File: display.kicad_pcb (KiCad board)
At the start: 2 copper layers, 154.4 x 18.8 mm, 43 parts, among them P1 USB, P10 NAV_TRANS, P11 NAV_ID, P12 NAV_VOL, P2 Power, P3 SPI Debug, P4 LED_JUMPER, P5 COM_ENC, P6 COM_STEP, P7 COM_TRANS, P8 COM_VOL, P9 NAV_ENC, U1 ATmega32U4, U10 RESET, U2 MAX7221, U3 5x7Segment, U4 MAX7221, U5 5x7Segment, U6 MAX7221, U7 5x7Segment, U8 MAX7221, U9 5x7Segment

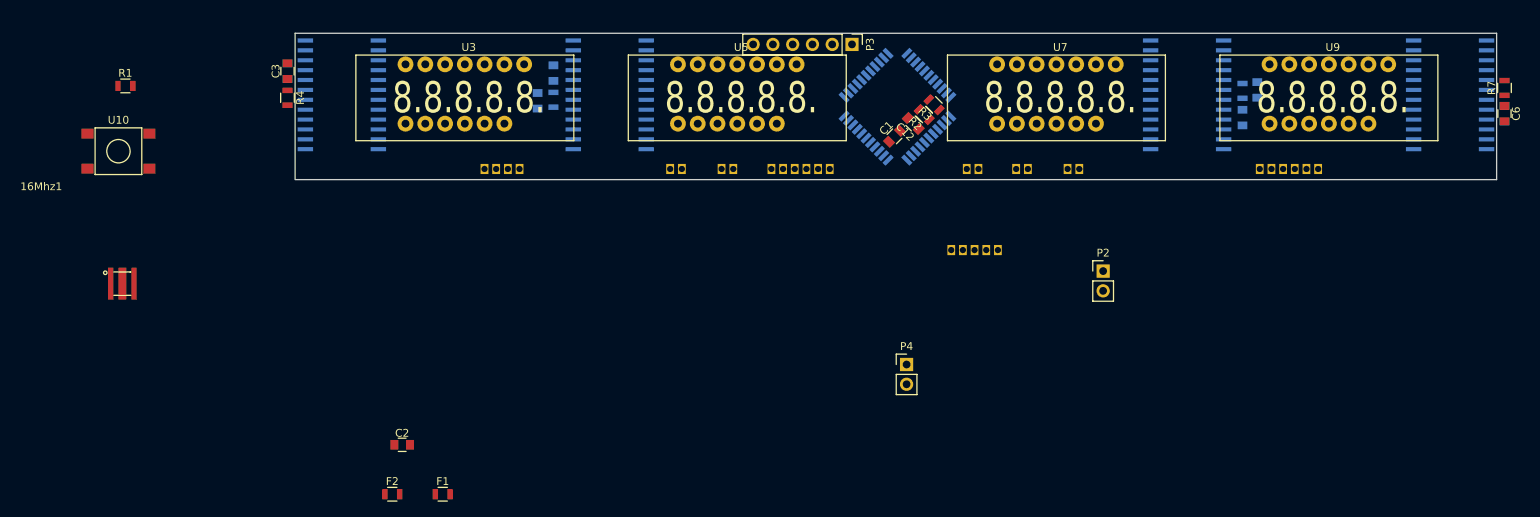
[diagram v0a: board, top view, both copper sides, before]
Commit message: Finished trace routing.  Added 3d parts
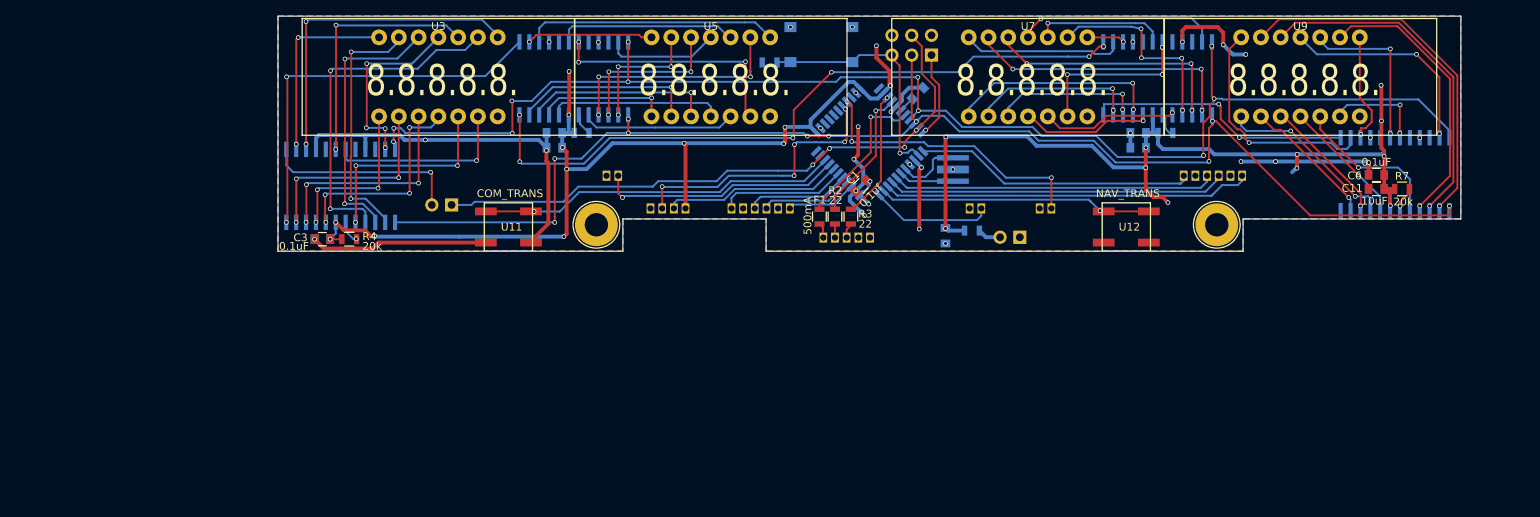
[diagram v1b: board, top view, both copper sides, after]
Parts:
- removed P10: NAV_TRANS, custom:JST-ZH-THRx2
- removed P7: COM_TRANS, custom:JST-ZH-THRx2
- added Ref**: Val**, custom:SCREW_4-40, F.Cu at (140.9, 126.8)
- added Ref**: Val**, custom:SCREW_4-40, F.Cu at (220.6, 126.8)
- added U11: COM_TRANS, custom:TAC_SWITCH_CK_KSC4_JWING, F.Cu at (129.6, 127.1)
- added U12: NAV_TRANS, custom:TAC_SWITCH_CK_KSC4_JWING, F.Cu at (209.0, 127.1)
- 16Mhz1, C12, C2, F2, R1, U10: moved to B.Cu
- C11: moved to F.Cu
- P2, P4: footprint Pin_Headers:Pin_Header_Straight_1x02_Pitch2.54mm -> custom:Pin_Header_Straight_1x02_Pitch2.54mm; moved to B.Cu
- P3: footprint Pin_Headers:Pin_Header_Straight_1x06_Pitch2.54mm -> custom:Pin_Header_Straight_2x03_Pitch2.54mm; moved to B.Cu
- U3, U5, U7, U9: value 5x7Segment -> 5x7Segment_0.36; footprint custom:5x7Segment -> custom:5x7Segment_0.36
- moved 16Mhz1 107.7 mm to (186.7, 119.7), turned to 90 degrees
- moved U10 91.3 mm to (169.8, 103.7)
- moved R1 82.8 mm to (163.2, 106.0), turned to 180 degrees
- moved F2 81.8 mm to (189.2, 127.5), turned to 180 degrees
- moved C2 74.8 mm to (185.8, 128.2), turned to 270 degrees
- moved P4 61.9 mm to (122.3, 124.2), turned to 90 degrees
- moved F1 60.1 mm to (169.6, 125.8), turned to 90 degrees
- moved C3 22.0 mm to (105.7, 128.7), turned to 180 degrees
- moved C8 22.0 mm to (105.7, 128.7), turned to 180 degrees
- moved P8 21.9 mm to (150.1, 124.7)
- moved R4 19.8 mm to (109.2, 128.7), turned to 0 degrees
- moved C11 19.1 mm to (241.1, 122.2), turned to 180 degrees
- moved R7 18.5 mm to (244.4, 122.2), turned to 0 degrees
- moved C6 18.2 mm to (241.1, 120.4), turned to 180 degrees
- moved R3 17.9 mm to (173.6, 125.8), turned to 270 degrees
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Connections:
- U1 pad 12: /COM_S_B -> /NAV_S_B
- U1 pad 18: /COM_PWR -> /NAV_S_A
- U1 pad 19: /NAV_L_A -> /NAV_L_B
- U1 pad 20: /NAV_L_B -> /NAV_L_A
- U1 pad 21: /NAV_S_A -> /NAV_TRANS
- U1 pad 22: /NAV_TRANS -> /NAV_ID
- U1 pad 25: /NAV_S_B -> /COM_L_A
- U1 pad 26: /NAV_ID -> /COM_L_B
- U1 pad 27: (no net) -> /COM_S_A
- U1 pad 28: /COM_L_A -> /COM_S_B
- U1 pad 29: /COM_L_B -> /COM_PWR
- U1 pad 30: /COM_S_A -> /COM_STEP
- U1 pad 31: /COM_STEP -> /COM_TRANS
- U1 pad 32: /COM_TRANS -> (no net)
- U1 pad 40: /NAV_VOL -> /COM_VOL
- U1 pad 41: /COM_VOL -> /NAV_VOL
- U10 pad 1: GND -> /RST
- U10 pad 4: /RST -> GND
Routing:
- net VCC: track 0.00 -> 253.3 mm, vias 0 -> 30
- net CS: track 0.00 -> 175.0 mm, vias 0 -> 11
- net CLK: track 0.00 -> 172.5 mm, vias 0 -> 10
- net GND: track 0.00 -> 114.8 mm, vias 0 -> 25
- net /NavActive/DIN: track 0.00 -> 90.1 mm, vias 0 -> 6
- net /MOSI: track 0.00 -> 79.0 mm, vias 0 -> 4
- net /ComStandby/DIN: track 0.00 -> 50.6 mm, vias 0 -> 2
- net /NAV_L_A: track 0.00 -> 47.5 mm
- net /NavStandby/S_A: track 0.00 -> 46.9 mm, vias 0 -> 1
- net /COM_TRANS: track 0.00 -> 46.3 mm, vias 0 -> 1
- net /ComActive/S_B: track 0.00 -> 44.5 mm, vias 0 -> 2
- net /NavStandby/S_F: track 0.00 -> 43.7 mm, vias 0 -> 1
- net /NAV_L_B: track 0.00 -> 43.5 mm
- net /ComActive/D_5: track 0.00 -> 42.2 mm, vias 0 -> 2
- net /NAV_S_A: track 0.00 -> 41.7 mm
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- added copper zone on F.Cu, net GND
- added copper zone on B.Cu, net VCC
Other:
- board size 154.4 x 18.8 mm -> 151.9 x 30.2 mm
- net class Power added: clearance 0.2, trace_width 0.5, via_dia 0.6, via_drill 0.4

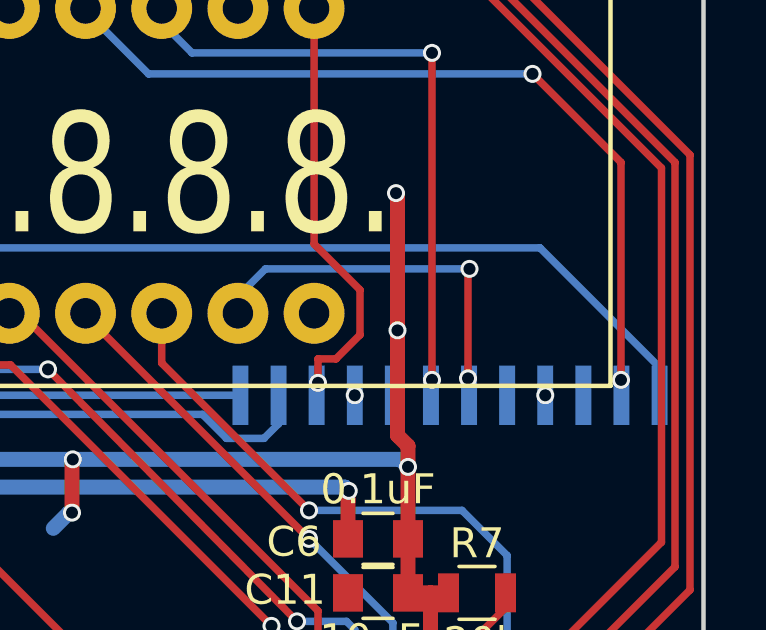
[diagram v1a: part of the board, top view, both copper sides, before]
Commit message: Fixed unconnected ground.
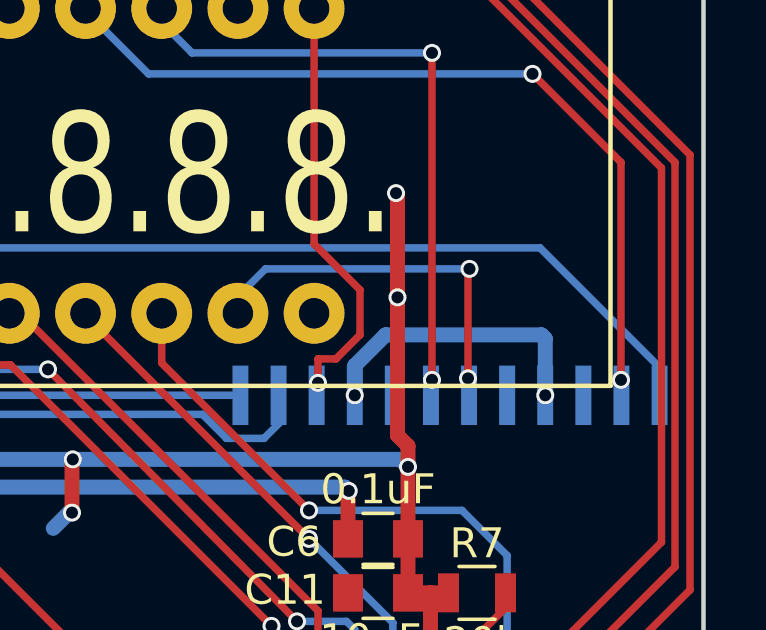
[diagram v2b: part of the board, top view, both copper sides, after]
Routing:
- net GND: track 114.8 -> 124.5 mm
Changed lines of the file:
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@@
   (general
     (links 170)
-    (no_connects 1)
+    (no_connects 0)
     (area 99.924999 99.924999 252.025001 130.275001)
     (thickness 1.6)
     (drawings 11)
-    (tracks 1115)
+    (tracks 1120)
     (zones 0)
     (modules 45)
@@
   (page A4)
   (layers
-    (0 F.Cu signal hide)
+    (0 F.Cu signal)
     (31 B.Cu signal)
     (32 B.Adhes user)
@@
   (segment (start 192.76 128.4) (end 190.95 128.4) (width 0.5) (layer B.Cu) (net 1))
   (segment (start 190.95 128.4) (end 190.1 127.55) (width 0.5) (layer B.Cu) (net 1))
+  (segment (start 246.675 115.6135) (end 246.675 113.725) (width 0.5) (layer B.Cu) (net 2))
+  (segment (start 241.35 113.6) (end 240.325 114.625) (width 0.5) (layer B.Cu) (net 2))
+  (segment (start 246.55 113.6) (end 241.35 113.6) (width 0.5) (layer B.Cu) (net 2))
+  (segment (start 246.675 113.725) (end 246.55 113.6) (width 0.5) (layer B.Cu) (net 2))
+  (segment (start 240.325 114.625) (end 240.325 115.6135) (width 0.5) (layer B.Cu) (net 2))
+  (segment (start 246.675 115.6135) (end 246.675 115.625) (width 0.5) (layer F.Cu) (net 2))
+  (via (at 246.675 115.6135) (size 0.6) (drill 0.4) (layers F.Cu B.Cu) (net 2))
+  (via (at 240.325 115.6135) (size 0.6) (drill 0.4) (layers F.Cu B.Cu) (net 2))
   (segment (start 216.175 103.3135) (end 216.175 101.85) (width 0.5) (layer F.Cu) (net 2))
   (segment (start 216.175 103.3) (end 216.175 103.3135) (width 0.5) (layer F.Cu) (net 2))
@@
   (via (at 240.125 118.8) (size 0.6) (drill 0.4) (layers F.Cu B.Cu) (net 2))
   (segment (start 240.1 118.825) (end 240.125 118.8) (width 0.5) (layer F.Cu) (net 2))
-  (via (at 246.675 115.6135) (size 0.6) (drill 0.4) (layers F.Cu B.Cu) (net 2))
-  (segment (start 246.675 115.6135) (end 246.675 115.625) (width 0.5) (layer F.Cu) (net 2))
-  (via (at 240.325 115.6135) (size 0.6) (drill 0.4) (layers F.Cu B.Cu) (net 2))
   (segment (start 240.325 115.6135) (end 240.325 115.625) (width 0.5) (layer F.Cu) (net 2))
   (via (at 185.75 129.2) (size 0.6) (drill 0.4) (layers F.Cu B.Cu) (net 2))
@@
   (segment (start 137.4 112.6515) (end 137.4 107.1) (width 0.5) (layer F.Cu) (net 3))
   (segment (start 137.365 112.6865) (end 137.4 112.6515) (width 0.5) (layer F.Cu) (net 3))
-  (segment (start 241.75 113.45) (end 241.75 108.925) (width 0.5) (layer F.Cu) (net 3))
+  (segment (start 241.75 112.35) (end 241.75 108.925) (width 0.5) (layer F.Cu) (net 3))
   (segment (start 242.1 117.3) (end 241.75 116.95) (width 0.5) (layer F.Cu) (net 3))
-  (segment (start 241.75 116.95) (end 241.75 113.45) (width 0.5) (layer F.Cu) (net 3))
-  (via (at 241.75 113.45) (size 0.6) (drill 0.4) (layers F.Cu B.Cu) (net 3))
+  (segment (start 241.75 116.95) (end 241.75 112.35) (width 0.5) (layer F.Cu) (net 3))
+  (via (at 241.75 112.35) (size 0.6) (drill 0.4) (layers F.Cu B.Cu) (net 3))
   (segment (start 242.1 118) (end 242.1 117.3) (width 0.5) (layer F.Cu) (net 3))
   (via (at 241.7 108.875) (size 0.6) (drill 0.4) (layers F.Cu B.Cu) (net 3))

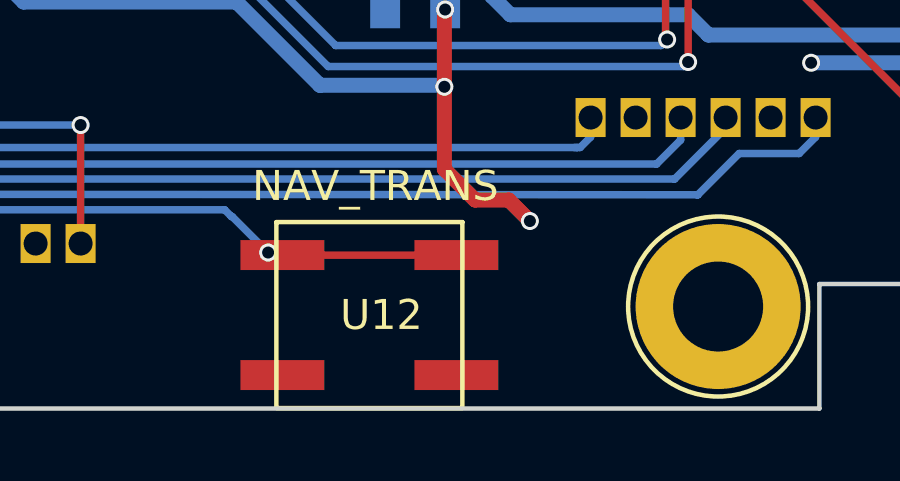
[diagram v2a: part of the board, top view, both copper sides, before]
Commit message: Added 3d footprints for tac switches and resonator.
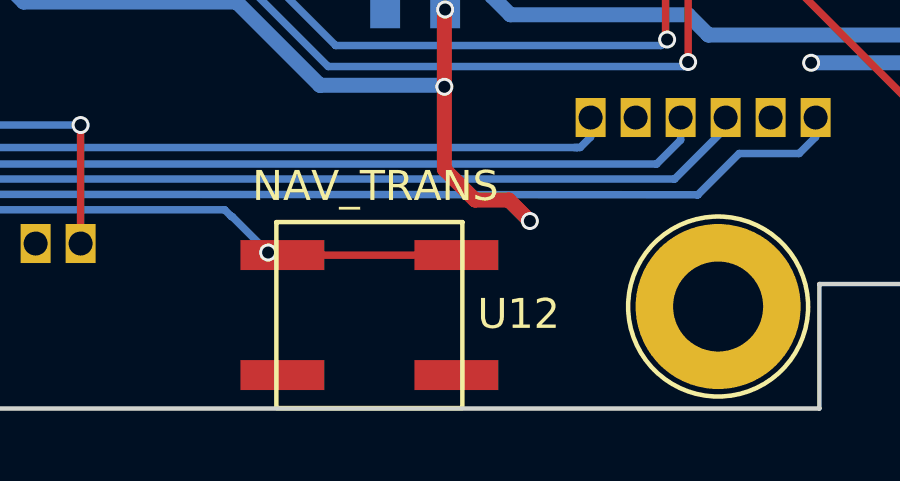
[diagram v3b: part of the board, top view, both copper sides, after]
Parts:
- removed 16Mhz1: CRYSTAL_SMD, custom:Oscilator_Cap_SMD
- added RS1: 16Mhz, custom:RESONATOR_SMD_Abracon_AWSCR, B.Cu at (186.7, 119.7)
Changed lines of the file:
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@@
     (add_net VCC)
-  )
-  (module custom:Oscilator_Cap_SMD (layer B.Cu)
-    (at 186.7 119.7 90)
-    (descr "Abracon AWSCR-16.00CV-T")
-    (tags oscilator)
-    (fp_text reference 16Mhz1 (at 2.85 1.625 360) (layer B.SilkS)
-      (effects (font (size 1 1) (thickness 0.15)) (justify mirror))
-    )
-    (fp_text value CRYSTAL_SMD (at 2.9 1.25 180) (layer B.SilkS) hide
-      (effects (font (size 1 1) (thickness 0.15)) (justify mirror))
-    )
-    (fp_line (start -1.1 -1.5) (end 1.1 -1.5) (layer B.SilkS) (width 0.15))
-    (fp_line (start -1.1 1.5) (end 1 1.5) (layer B.SilkS) (width 0.15))
-    (fp_line (start 1 1.5) (end 1.1 1.5) (layer B.SilkS) (width 0.15))
-    (fp_circle (center -2.2 1.4) (end -2.1 1.6) (layer B.SilkS) (width 0.15))
-    (pad 1 smd rect (at -1.5 0 90) (size 0.7 4.1) (layers B.Cu B.Paste B.Mask)
-      (net 4 /XTAL1))
-    (pad 2 smd rect (at 1.5 0 90) (size 0.7 4.1) (layers B.Cu B.Paste B.Mask)
-      (net 5 /XTAL2))
-    (pad 3 smd rect (at 0 0 90) (size 1 4.1) (layers B.Cu B.Paste B.Mask)
-      (net 2 GND))
   )
   (module Capacitors_SMD:C_0805 (layer F.Cu)
@@
       (rotate (xyz 0 0 0))
     )
-  )
-  (module custom:TAC_SWITCH_CK_KSC4_JWING (layer F.Cu)
-    (at 129.6 127.085)
-    (fp_text reference U11 (at 0.4 0) (layer F.SilkS)
-      (effects (font (size 1 1) (thickness 0.15)))
-    )
-    (fp_text value COM_TRANS (at 0.2 -4.3) (layer F.SilkS)
-      (effects (font (size 1 1) (thickness 0.15)))
-    )
-    (fp_line (start -3.1 -3.1) (end 3.1 -3.1) (layer F.SilkS) (width 0.15))
-    (fp_line (start 3.1 -3.1) (end 3.1 3.1) (layer F.SilkS) (width 0.15))
-    (fp_line (start 3.1 3.1) (end -3.1 3.1) (layer F.SilkS) (width 0.15))
-    (fp_line (start -3.1 3.1) (end -3.1 -3.1) (layer F.SilkS) (width 0.15))
-    (pad 4 smd rect (at 2.9 2) (size 2.8 1) (layers F.Cu F.Paste F.Mask)
-      (net 2 GND))
-    (pad 3 smd rect (at -2.9 2) (size 2.8 1) (layers F.Cu F.Paste F.Mask)
-      (net 2 GND))
-    (pad 2 smd rect (at 2.9 -2) (size 2.8 1) (layers F.Cu F.Paste F.Mask)
-      (net 19 /COM_TRANS))
-    (pad 1 smd rect (at -2.9 -2) (size 2.8 1) (layers F.Cu F.Paste F.Mask)
-      (net 19 /COM_TRANS))
-  )
-  (module custom:TAC_SWITCH_CK_KSC4_JWING (layer F.Cu)
-    (at 208.975 127.085)
-    (fp_text reference U12 (at 0.4 0) (layer F.SilkS)
-      (effects (font (size 1 1) (thickness 0.15)))
-    )
-    (fp_text value NAV_TRANS (at 0.2 -4.3) (layer F.SilkS)
-      (effects (font (size 1 1) (thickness 0.15)))
-    )
-    (fp_line (start -3.1 -3.1) (end 3.1 -3.1) (layer F.SilkS) (width 0.15))
-    (fp_line (start 3.1 -3.1) (end 3.1 3.1) (layer F.SilkS) (width 0.15))
-    (fp_line (start 3.1 3.1) (end -3.1 3.1) (layer F.SilkS) (width 0.15))
-    (fp_line (start -3.1 3.1) (end -3.1 -3.1) (layer F.SilkS) (width 0.15))
-    (pad 4 smd rect (at 2.9 2) (size 2.8 1) (layers F.Cu F.Paste F.Mask)
-      (net 2 GND))
-    (pad 3 smd rect (at -2.9 2) (size 2.8 1) (layers F.Cu F.Paste F.Mask)
-      (net 2 GND))
-    (pad 2 smd rect (at 2.9 -2) (size 2.8 1) (layers F.Cu F.Paste F.Mask)
-      (net 26 /NAV_TRANS))
-    (pad 1 smd rect (at -2.9 -2) (size 2.8 1) (layers F.Cu F.Paste F.Mask)
-      (net 26 /NAV_TRANS))
   )
   (module custom:SCREW_4-40 (layer F.Cu)
@@
     )
   )
+  (module custom:TAC_SWITCH_CK_KSC4_JWING (layer F.Cu)
+    (at 208.975 127.085)
+    (fp_text reference U12 (at 4.975 -0.035) (layer F.SilkS)
+      (effects (font (size 1 1) (thickness 0.15)))
+    )
+    (fp_text value NAV_TRANS (at 0.2 -4.3) (layer F.SilkS)
+      (effects (font (size 1 1) (thickness 0.15)))
+    )
+    (fp_line (start -3.1 -3.1) (end 3.1 -3.1) (layer F.SilkS) (width 0.15))
+    (fp_line (start 3.1 -3.1) (end 3.1 3.1) (layer F.SilkS) (width 0.15))
+    (fp_line (start 3.1 3.1) (end -3.1 3.1) (layer F.SilkS) (width 0.15))
+    (fp_line (start -3.1 3.1) (end -3.1 -3.1) (layer F.SilkS) (width 0.15))
+    (pad 4 smd rect (at 2.9 2) (size 2.8 1) (layers F.Cu F.Paste F.Mask)
+      (net 2 GND))
+    (pad 3 smd rect (at -2.9 2) (size 2.8 1) (layers F.Cu F.Paste F.Mask)
+      (net 2 GND))
+    (pad 2 smd rect (at 2.9 -2) (size 2.8 1) (layers F.Cu F.Paste F.Mask)
+      (net 26 /NAV_TRANS))
+    (pad 1 smd rect (at -2.9 -2) (size 2.8 1) (layers F.Cu F.Paste F.Mask)
+      (net 26 /NAV_TRANS))
+    (model ${CUSTOM_LIB}/custom.3dshapes/TAC_SWITCH_CK_KSC4_J.wrl
+      (at (xyz 0 0 0))
+      (scale (xyz 0.3937 0.3937 0.3937))
+      (rotate (xyz 0 0 0))
+    )
+  )
+  (module custom:TAC_SWITCH_CK_KSC4_JWING (layer F.Cu)
+    (at 129.6 127.085)
+    (fp_text reference U11 (at 0.4 0) (layer F.SilkS)
+      (effects (font (size 1 1) (thickness 0.15)))
+    )
+    (fp_text value COM_TRANS (at 0.2 -4.3) (layer F.SilkS)
+      (effects (font (size 1 1) (thickness 0.15)))
+    )
+    (fp_line (start -3.1 -3.1) (end 3.1 -3.1) (layer F.SilkS) (width 0.15))
+    (fp_line (start 3.1 -3.1) (end 3.1 3.1) (layer F.SilkS) (width 0.15))
+    (fp_line (start 3.1 3.1) (end -3.1 3.1) (layer F.SilkS) (width 0.15))
+    (fp_line (start -3.1 3.1) (end -3.1 -3.1) (layer F.SilkS) (width 0.15))
+    (pad 4 smd rect (at 2.9 2) (size 2.8 1) (layers F.Cu F.Paste F.Mask)
+      (net 2 GND))
+    (pad 3 smd rect (at -2.9 2) (size 2.8 1) (layers F.Cu F.Paste F.Mask)
+      (net 2 GND))
+    (pad 2 smd rect (at 2.9 -2) (size 2.8 1) (layers F.Cu F.Paste F.Mask)
+      (net 19 /COM_TRANS))
+    (pad 1 smd rect (at -2.9 -2) (size 2.8 1) (layers F.Cu F.Paste F.Mask)
+      (net 19 /COM_TRANS))
+    (model ${CUSTOM_LIB}/custom.3dshapes/TAC_SWITCH_CK_KSC4_J.wrl
+      (at (xyz 0 0 0))
+      (scale (xyz 0.3937 0.3937 0.3937))
+      (rotate (xyz 0 0 0))
+    )
+  )
+  (module custom:RESONATOR_SMD_Abracon_AWSCR (layer B.Cu)
+    (at 186.7 119.7 90)
+    (descr "Abracon AWSCR")
+    (tags resonator)
+    (fp_text reference RS1 (at 0.45 3.1 90) (layer B.SilkS)
+      (effects (font (size 1 1) (thickness 0.15)) (justify mirror))
+    )
+    (fp_text value 16Mhz (at 2.9 0.5 180) (layer B.SilkS)
+      (effects (font (size 1 1) (thickness 0.15)) (justify mirror))
+    )
+    (fp_line (start -1.1 -1.5) (end 1.1 -1.5) (layer B.SilkS) (width 0.15))
+    (fp_line (start -1.1 1.5) (end 1 1.5) (layer B.SilkS) (width 0.15))
+    (fp_line (start 1 1.5) (end 1.1 1.5) (layer B.SilkS) (width 0.15))
+    (fp_circle (center -2.2 1.4) (end -2.1 1.6) (layer B.SilkS) (width 0.15))
+    (pad 1 smd rect (at -1.5 0 90) (size 0.7 4.1) (layers B.Cu B.Paste B.Mask)
+      (net 4 /XTAL1))
+    (pad 2 smd rect (at 1.5 0 90) (size 0.7 4.1) (layers B.Cu B.Paste B.Mask)
+      (net 5 /XTAL2))
+    (pad 3 smd rect (at 0 0 90) (size 1 4.1) (layers B.Cu B.Paste B.Mask)
+      (net 2 GND))
+    (model ${CUSTOM_LIB}/custom.3dshapes/RESONATOR_SMD_Abracon_AWSCR.wrl
+      (at (xyz 0 0 0))
+      (scale (xyz 0.3937 0.3937 0.3937))
+      (rotate (xyz 0 0 0))
+    )
+  )
   (gr_line (start 223.975 130.2) (end 162.7 130.2) (angle 90) (layer Edge.Cuts) (width 0.15))
   (gr_line (start 144.3 130.2) (end 100 130.2) (angle 90) (layer Edge.Cuts) (width 0.15))
@@
   (segment (start 192.76 128.4) (end 190.95 128.4) (width 0.5) (layer B.Cu) (net 1))
   (segment (start 190.95 128.4) (end 190.1 127.55) (width 0.5) (layer B.Cu) (net 1))
+  (via (at 186.7 119.7) (size 0.6) (drill 0.4) (layers F.Cu B.Cu) (net 2))
   (segment (start 246.675 115.6135) (end 246.675 113.725) (width 0.5) (layer B.Cu) (net 2))
   (segment (start 241.35 113.6) (end 240.325 114.625) (width 0.5) (layer B.Cu) (net 2))
@@
   (segment (start 174.797918 123.047918) (end 175.9 124.15) (width 0.5) (layer B.Cu) (net 2))
   (via (at 175.9 124.15) (size 0.6) (drill 0.4) (layers F.Cu B.Cu) (net 2))
-  (via (at 186.7 119.7) (size 0.6) (drill 0.4) (layers F.Cu B.Cu) (net 2))
   (segment (start 181.175 119.05) (end 181.162742 119.05) (width 0.5) (layer F.Cu) (net 2))
   (segment (start 181.162742 119.05) (end 181.16188 119.049138) (width 0.5) (layer F.Cu) (net 2))
